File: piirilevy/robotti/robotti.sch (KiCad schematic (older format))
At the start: 1 part

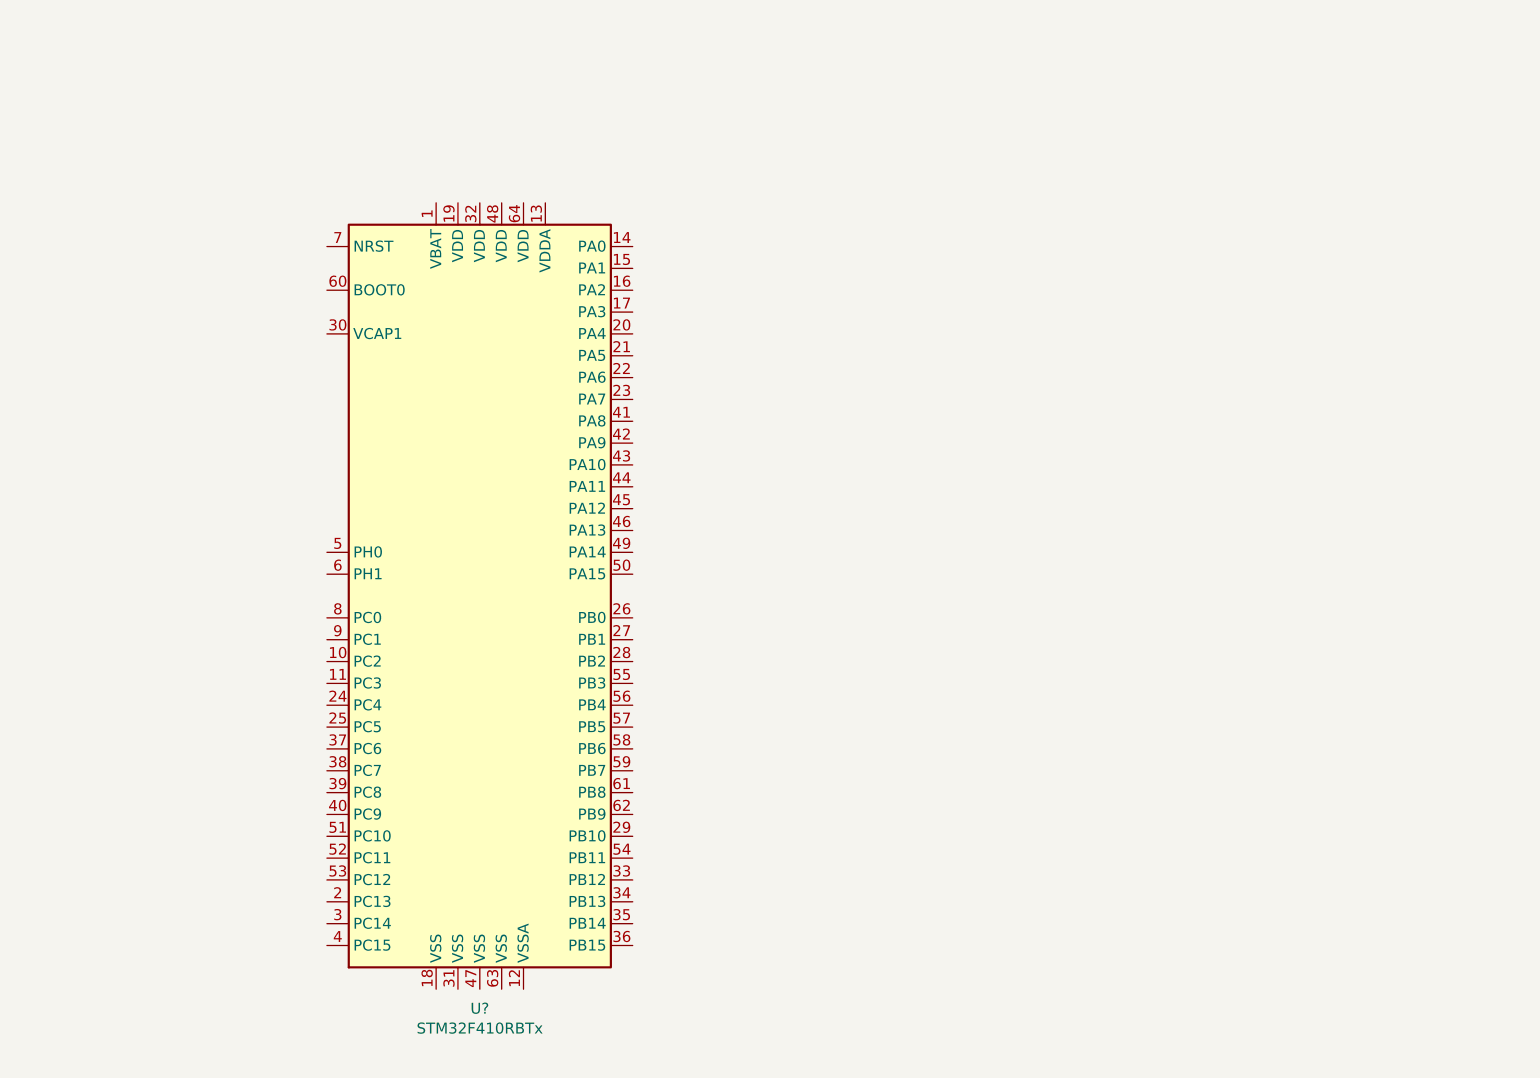
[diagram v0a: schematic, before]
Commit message: MCU lisätty, jännitesyöttö ja kide
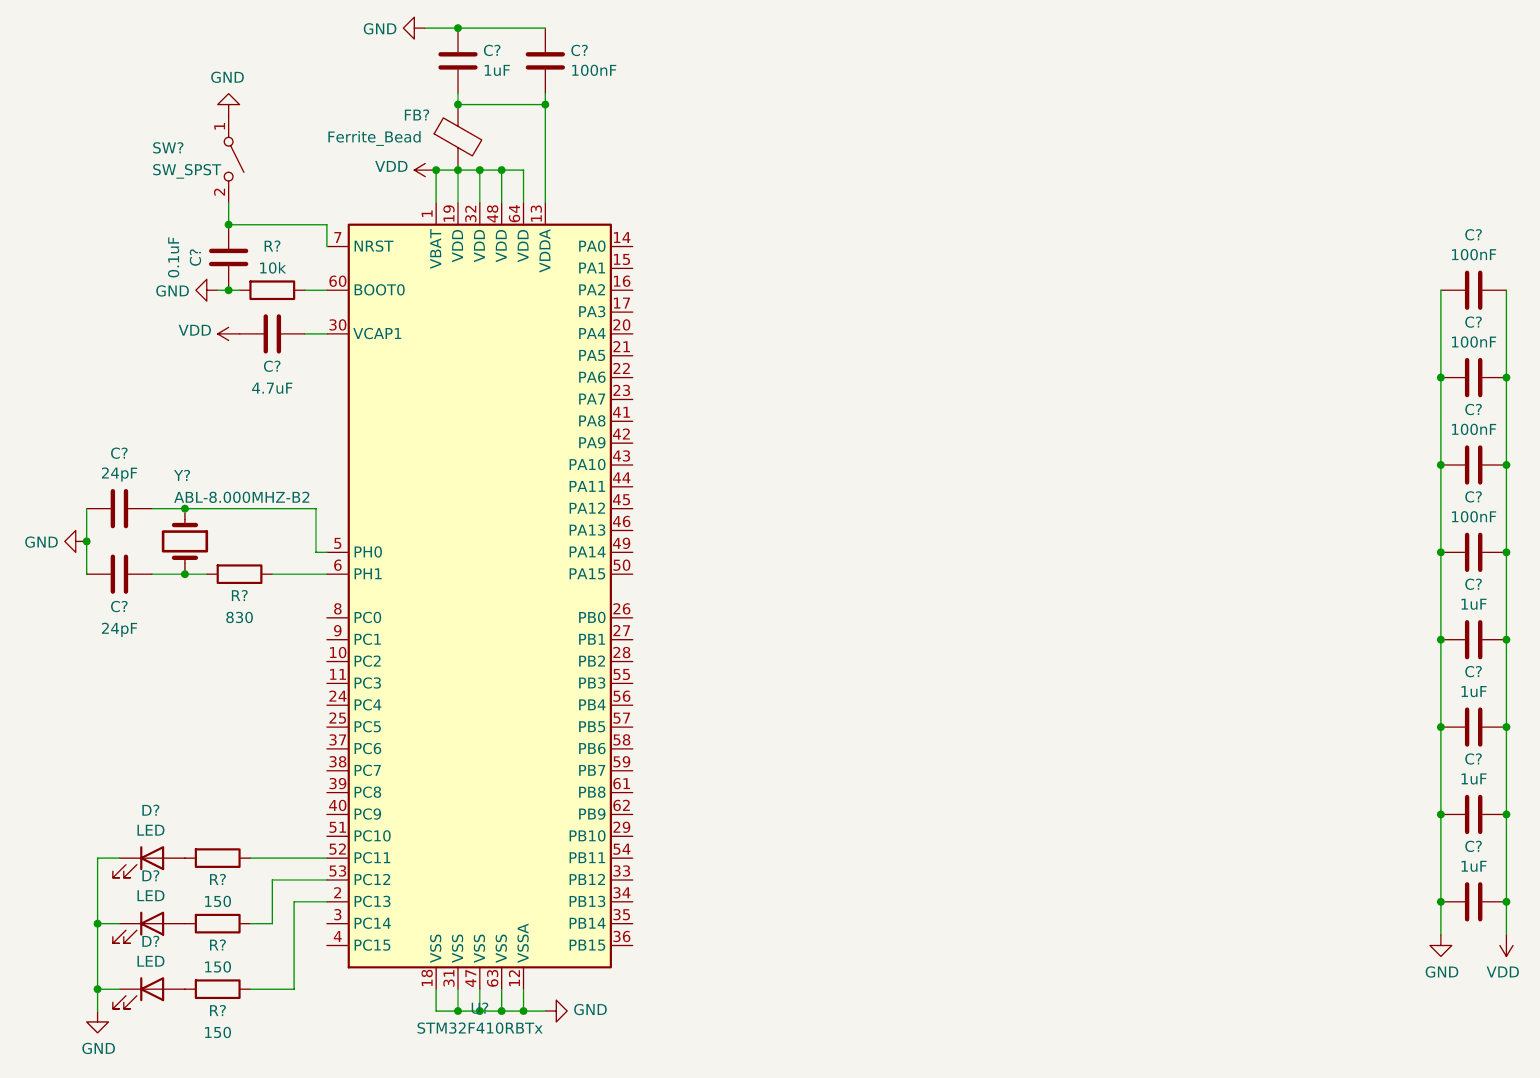
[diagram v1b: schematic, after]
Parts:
- added C? (x5): 1uF, symbol Device:C
- added C? (x5): 100nF, symbol Device:C
- added C? (x2): 24pF, symbol Device:C
- added C?: 4.7uF, symbol Device:C
- added C?: 0.1uF, symbol Device:C
- added D? (x3): LED, symbol Device:LED
- added FB?: Ferrite_Bead, symbol Device:Ferrite_Bead
- added R?: 830, symbol Device:R
- added R?: 10k, symbol Device:R
- added R? (x3): 150, symbol Device:R
- added SW?: SW_SPST, symbol Switch:SW_SPST
- added Y?: ABL-8.000MHZ-B2, symbol Device:Crystal
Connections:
- net VDD: now reaches U?.1 (VBAT)
- net VDD: now also U?.19 (VDD), U?.32 (VDD), U?.48 (VDD), U?.64 (VDD), C?.1, C?.1, C?.1, C?.1, C?.1, C?.2, C?.2, C?.2, C?.2, FB?.2
- net GND: now reaches U?.12 (VSSA)
- net GND: now also U?.18 (VSS), U?.31 (VSS), U?.47 (VSS), U?.63 (VSS), C?.1, C?.1, C?.1, C?.1, C?.1, C?.1, C?.2, C?.2, C?.2, C?.2, C?.2, C?.2, C?.2, D?.1 (K), D?.1 (K), D?.1 (K), R?.2, SW?.1 (A)
- net at U?.13 (VDDA): now also C?.2, C?.2, FB?.1
- net at U?.2 (PC13): now also R?.1
- net at U?.30 (VCAP1): now also C?.2
- net at U?.5 (PH0): now also C?.1, Y?.1
- net at U?.52 (PC11): now also R?.1
- net at U?.53 (PC12): now also R?.1
- net at U?.6 (PH1): now also R?.1
- net at U?.60 (BOOT0): now also R?.1
- net at U?.7 (NRST): now also C?.1, SW?.2 (B)
- new net: C?.1, R?.2, Y?.2
- new net: D?.2 (A), R?.2 (x3)

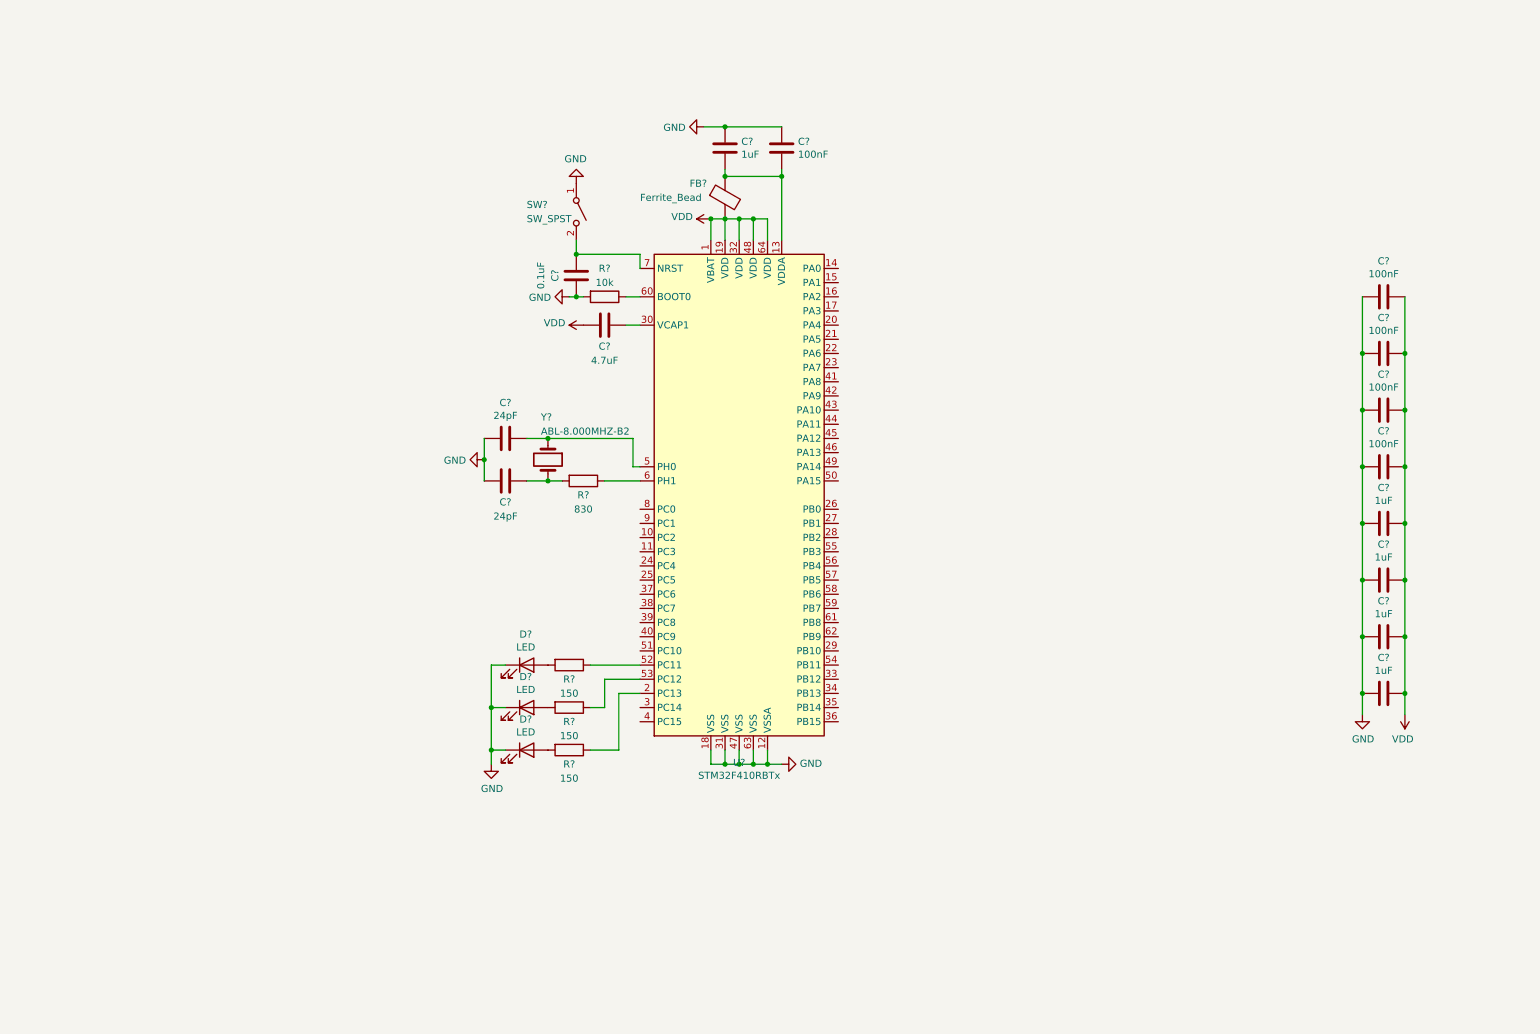
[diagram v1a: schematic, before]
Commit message: Lisätty LoRa, etäisyys, lämpö- ja valoisuusanturi
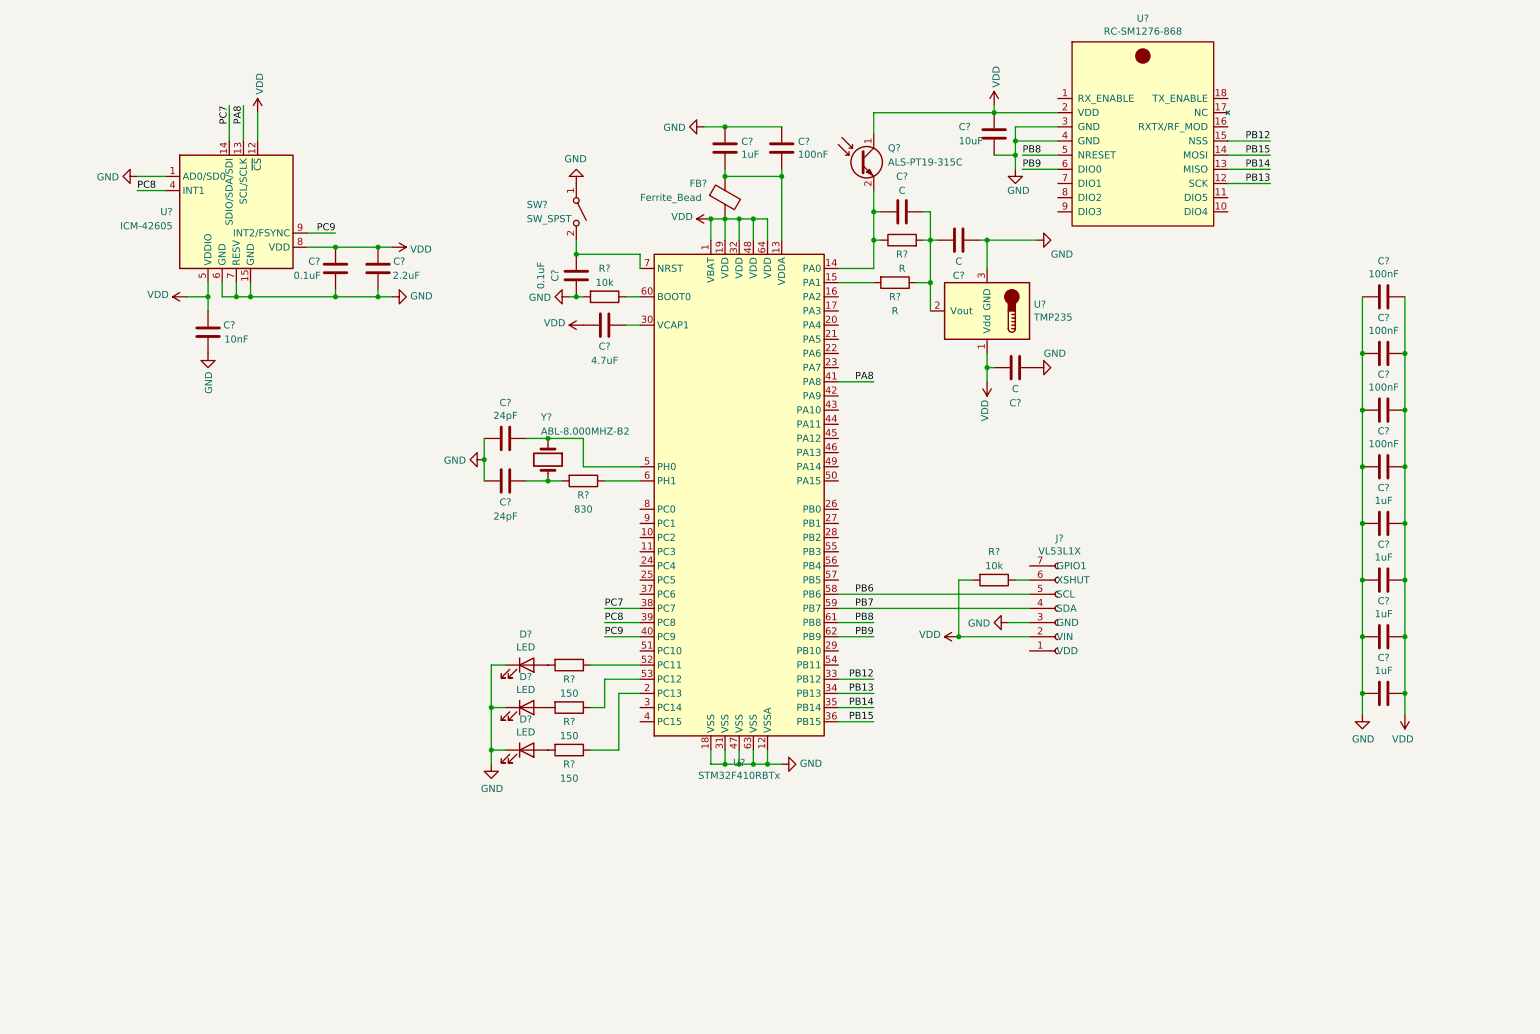
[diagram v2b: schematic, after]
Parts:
- added C?: 0.1uF, symbol Device:C
- added C?: 2.2uF, symbol Device:C
- added C?: 10nF, symbol Device:C
- added C?: 10uF, symbol Device:C
- added C? (x3): C, symbol Device:C
- added J?: VL53L1X, Connector_JST:JST_XH_B7B-XH-AM_1x07_P2.50mm_Vertical, symbol robotti_library:VL53L1X
- added Q?: ALS-PT19-315C, Diode_SMD:D_1206_3216Metric_Pad1.42x1.75mm_HandSolder, symbol robotti_library:ALS-PT19-315C
- added R?: 10k, symbol Device:R
- added R? (x2): R, symbol Device:R
- added U?: ICM-42605, Package_LGA:LGA-14_3x2.5mm_P0.5mm_LayoutBorder3x4y, symbol robotti_library:ICM-42605
- added U?: RC-SM1276-868, symbol robotti_library:RC-SM1276-868
- added U?: TMP235, Package_TO_SOT_SMD:SOT-323_SC-70, symbol robotti_library:TMP235
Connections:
- net GND: now also C?.1, C?.1, C?.2, C?.2, C?.2, C?.2, J?.3 (GND), U?.1 (AD0/SD0), U?.15 (GND), U?.3 (GND), U?.3 (GND), U?.4 (GND), U?.6 (GND), U?.7 (RESV)
- net VDD: now also C?.1, C?.1, C?.1, C?.1, C?.2, J?.2 (VIN), Q?.1 (C), R?.2, U?.1 (Vdd), U?.12 (~CS), U?.2 (VDD), U?.5 (VDDIO), U?.8 (VDD)
- net at U?.14 (PA0): now also C?.1, Q?.2 (E), R?.1
- net at U?.15 (PA1): now also R?.2
- net PB12: now reaches U?.33 (PB12)
- net PB12: now also U?.15 (NSS)
- net PB13: now reaches U?.34 (PB13)
- net PB13: now also U?.12 (SCK)
- net PB14: now reaches U?.35 (PB14)
- net PB14: now also U?.13 (MISO)
- net PB15: now reaches U?.36 (PB15)
- net PB15: now also U?.14 (MOSI)
- net PC7: now reaches U?.38 (PC7)
- net PC7: now also U?.14 (SDIO/SDA/SDI)
- net PC8: now reaches U?.39 (PC8)
- net PC8: now also U?.4 (INT1)
- net PC9: now reaches U?.40 (PC9)
- net PC9: now also U?.9 (INT2/FSYNC)
- net PA8: now reaches U?.41 (PA8)
- net PA8: now also U?.13 (SCL/SCLK)
- net PB6: now reaches U?.58 (PB6)
- net PB6: now also J?.5 (SCL)
- net PB7: now reaches U?.59 (PB7)
- net PB7: now also J?.4 (SDA)
- net PB8: now reaches U?.61 (PB8)
- net PB8: now also U?.5 (NRESET)
- net PB9: now reaches U?.62 (PB9)
- net PB9: now also U?.6 (DIO0)
- new net: J?.6 (XSHUT), R?.1
- new net: C?.2, C?.2, R?.1, R?.2, U?.2 (Vout)
